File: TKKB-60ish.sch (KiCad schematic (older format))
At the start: 1 part

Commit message: EOD 12-20-20
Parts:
- removed U?: ATmega32U4-AU, Package_QFP:TQFP-44_10x10mm_P0.8mm, symbol MCU_Microchip_ATmega:ATmega32U4-AU
- added C? (x2): 27pF, Capacitor_THT:CP_Radial_D6.3mm_P2.50mm, symbol Device:C_Small
- added U?: ATmega32A-PU, Package_DIP:DIP-40_W15.24mm, symbol MCU_Microchip_ATmega:ATmega32A-PU
- added Y?: 16MHz, Crystal:Crystal_HC49-U_Vertical, symbol Device:Crystal_Small
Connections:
- net labels added: GND
- wire segments 0 -> 8
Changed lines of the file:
@@
 $EndDescr
 $Comp
-L MCU_Microchip_ATmega:ATmega32U4-AU U?
-U 1 1 5FE000C5
-P 8650 3450
-F 0 "U?" H 8650 1561 50  0000 C CNN
-F 1 "ATmega32U4-AU" H 8650 1470 50  0000 C CNN
-F 2 "Package_QFP:TQFP-44_10x10mm_P0.8mm" H 8650 3450 50  0001 C CIN
-F 3 "http://ww1.microchip.com/downloads/en/DeviceDoc/Atmel-7766-8-bit-AVR-ATmega16U4-32U4_Datasheet.pdf" H 8650 3450 50  0001 C CNN
-	1    8650 3450
+L MCU_Microchip_ATmega:ATmega32A-PU U?
+U 1 1 5FE02254
+P 9450 3400
+F 0 "U?" H 9450 1311 50  0000 C CNN
+F 1 "ATmega32A-PU" H 9450 1220 50  0000 C CNN
+F 2 "Package_DIP:DIP-40_W15.24mm" H 9450 3400 50  0001 C CIN
+F 3 "http://ww1.microchip.com/downloads/en/DeviceDoc/atmel-8155-8-bit-microcontroller-avr-atmega32a_datasheet.pdf" H 9450 3400 50  0001 C CNN
+	1    9450 3400
 	1    0    0    -1
 $EndComp
+$Comp
+L Device:Crystal_Small Y?
+U 1 1 5FE087F5
+P 8200 2000
+F 0 "Y?" V 8154 2088 50  0000 L CNN
+F 1 "16MHz" V 8245 2088 50  0000 L CNN
+F 2 "Crystal:Crystal_HC49-U_Vertical" H 8200 2000 50  0001 C CNN
+F 3 "~" H 8200 2000 50  0001 C CNN
+	1    8200 2000
+	0    1    1    0
+$EndComp
+Wire Wire Line
+	8850 1900 8200 1900
+Wire Wire Line
+	8850 2100 8200 2100
+Connection ~ 8200 1900
+Connection ~ 8200 2100
+$Comp
+L Device:C_Small C?
+U 1 1 5FE0A369
+P 7850 1800
+F 0 "C?" H 7758 1754 50  0000 R CNN
+F 1 "27pF" H 7758 1845 50  0000 R CNN
+F 2 "Capacitor_THT:CP_Radial_D6.3mm_P2.50mm" H 7850 1800 50  0001 C CNN
+F 3 "~" H 7850 1800 50  0001 C CNN
+	1    7850 1800
+	-1   0    0    1
+$EndComp
+Wire Wire Line
+	7850 1900 8200 1900
+Wire Wire Line
+	7850 2100 8200 2100
+Wire Wire Line
+	7850 1700 7700 1700
+Wire Wire Line
+	7700 1700 7700 2300
+Wire Wire Line
+	7850 2300 7700 2300
+Connection ~ 7700 2300
+Wire Wire Line
+	7700 2300 7700 2450
+$Comp
+L power:GND #PWR?
+U 1 1 5FE0CB4E
+P 7700 2450
+F 0 "#PWR?" H 7700 2200 50  0001 C CNN
+F 1 "GND" H 7705 2277 50  0000 C CNN
+F 2 "" H 7700 2450 50  0001 C CNN
+F 3 "" H 7700 2450 50  0001 C CNN
+	1    7700 2450
+	1    0    0    -1
+$EndComp
+$Comp
+L Device:C_Small C?
+U 1 1 5FE0CF1A
+P 7850 2200
+F 0 "C?" H 7758 2154 50  0000 R CNN
+F 1 "27pF" H 7758 2245 50  0000 R CNN
+F 2 "Capacitor_THT:CP_Radial_D6.3mm_P2.50mm" H 7850 2200 50  0001 C CNN
+F 3 "~" H 7850 2200 50  0001 C CNN
+	1    7850 2200
+	-1   0    0    1
+$EndComp
 $EndSCHEMATC

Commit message: Schematic Updated - still in work
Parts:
- removed C? (x2): 27pF, Capacitor_THT:CP_Radial_D6.3mm_P2.50mm, symbol Device:C_Small
- removed U?: ATmega32A-PU, Package_DIP:DIP-40_W15.24mm, symbol MCU_Microchip_ATmega:ATmega32A-PU
- removed Y?: 16MHz, Crystal:Crystal_HC49-U_Vertical, symbol Device:Crystal_Small
- added C? (x3): 0.1uF, symbol Device:C_Small
- added C?: 10uF, symbol Device:C_Small
- added D?: D_Small, symbol Device:D_Small
- added MX?: MX-NoLED, Button_Switch_Keyboard:SW_Cherry_MX_1.00u_PCB, symbol MX_Alps_Hybrid:MX-NoLED
- added R? (x2): R_Small, symbol Device:R_Small
- added U?: ATmega32U4-AU, Package_QFP:TQFP-44_10x10mm_P0.8mm, symbol MCU_Microchip_ATmega:ATmega32U4-AU
- added Y?: 16MHz, symbol Device:Crystal_Small
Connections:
- net labels added: Col0, Row0
- net labels removed: GND
- wire segments 8 -> 5
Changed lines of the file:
@@
 EESchema Schematic File Version 4
+LIBS:TKKB-60ish-cache
 EELAYER 30 0
 EELAYER END
@@
 encoding utf-8
 Sheet 1 1
-Title ""
+Title "TKKB 60ISH"
 Date ""
-Rev ""
+Rev "v0.1"
 Comp ""
-Comment1 ""
+Comment1 "by Tim Klimpel"
 Comment2 ""
 Comment3 ""
@@
 $EndDescr
 $Comp
-L MCU_Microchip_ATmega:ATmega32A-PU U?
-U 1 1 5FE02254
-P 9450 3400
-F 0 "U?" H 9450 1311 50  0000 C CNN
-F 1 "ATmega32A-PU" H 9450 1220 50  0000 C CNN
-F 2 "Package_DIP:DIP-40_W15.24mm" H 9450 3400 50  0001 C CIN
-F 3 "http://ww1.microchip.com/downloads/en/DeviceDoc/atmel-8155-8-bit-microcontroller-avr-atmega32a_datasheet.pdf" H 9450 3400 50  0001 C CNN
-	1    9450 3400
+L MCU_Microchip_ATmega:ATmega32U4-AU U?
+U 1 1 5FE50288
+P 9600 3250
+F 0 "U?" H 9600 1361 50  0000 C CNN
+F 1 "ATmega32U4-AU" H 9600 1270 50  0000 C CNN
+F 2 "Package_QFP:TQFP-44_10x10mm_P0.8mm" H 9600 3250 50  0001 C CIN
+F 3 "http://ww1.microchip.com/downloads/en/DeviceDoc/Atmel-7766-8-bit-AVR-ATmega16U4-32U4_Datasheet.pdf" H 9600 3250 50  0001 C CNN
+	1    9600 3250
 	1    0    0    -1
 $EndComp
 $Comp
+L MX_Alps_Hybrid:MX-NoLED MX?
+U 1 1 5FE574F6
+P 1250 1600
+F 0 "MX?" H 1283 1823 60  0000 C CNN
+F 1 "MX-NoLED" H 1283 1749 20  0000 C CNN
+F 2 "Button_Switch_Keyboard:SW_Cherry_MX_1.00u_PCB" H 625 1575 60  0001 C CNN
+F 3 "" H 625 1575 60  0001 C CNN
+	1    1250 1600
+	1    0    0    -1
+$EndComp
+$Comp
+L Device:D_Small D?
+U 1 1 5FE5851E
+P 1200 2000
+F 0 "D?" V 1246 1932 50  0000 R CNN
+F 1 "D_Small" V 1155 1932 50  0000 R CNN
+F 2 "" V 1200 2000 50  0001 C CNN
+F 3 "~" V 1200 2000 50  0001 C CNN
+	1    1200 2000
+	0    -1   -1   0
+$EndComp
+Wire Wire Line
+	1200 1750 1200 1900
+Wire Wire Line
+	1400 1550 1750 1550
+Wire Wire Line
+	1200 2100 1200 2250
+Text GLabel 1750 1250 1    50   Input ~ 0
+Col0
+Wire Wire Line
+	1750 1550 1750 1250
+Text GLabel 1050 2250 0    50   Input ~ 0
+Row0
+Wire Wire Line
+	1200 2250 1050 2250
+$Comp
 L Device:Crystal_Small Y?
-U 1 1 5FE087F5
-P 8200 2000
-F 0 "Y?" V 8154 2088 50  0000 L CNN
-F 1 "16MHz" V 8245 2088 50  0000 L CNN
-F 2 "Crystal:Crystal_HC49-U_Vertical" H 8200 2000 50  0001 C CNN
-F 3 "~" H 8200 2000 50  0001 C CNN
-	1    8200 2000
+U 1 1 5FE5B267
+P 8450 2050
+F 0 "Y?" H 8450 2275 50  0000 C CNN
+F 1 "16MHz" H 8450 2184 50  0000 C CNN
+F 2 "" H 8450 2050 50  0001 C CNN
+F 3 "~" H 8450 2050 50  0001 C CNN
+	1    8450 2050
+	1    0    0    -1
+$EndComp
+$Comp
+L Device:R_Small R?
+U 1 1 5FE5BC3F
+P 8450 2750
+F 0 "R?" V 8254 2750 50  0000 C CNN
+F 1 "R_Small" V 8345 2750 50  0000 C CNN
+F 2 "" H 8450 2750 50  0001 C CNN
+F 3 "~" H 8450 2750 50  0001 C CNN
+	1    8450 2750
 	0    1    1    0
 $EndComp
-Wire Wire Line
-	8850 1900 8200 1900
-Wire Wire Line
-	8850 2100 8200 2100
-Connection ~ 8200 1900
-Connection ~ 8200 2100
+$Comp
+L Device:R_Small R?
+U 1 1 5FE5C705
+P 8150 2850
+F 0 "R?" V 7954 2850 50  0000 C CNN
+F 1 "R_Small" V 8045 2850 50  0000 C CNN
+F 2 "" H 8150 2850 50  0001 C CNN
+F 3 "~" H 8150 2850 50  0001 C CNN
+	1    8150 2850
+	0    1    1    0
+$EndComp
 $Comp
 L Device:C_Small C?
-U 1 1 5FE0A369
-P 7850 1800
-F 0 "C?" H 7758 1754 50  0000 R CNN
-F 1 "27pF" H 7758 1845 50  0000 R CNN
-F 2 "Capacitor_THT:CP_Radial_D6.3mm_P2.50mm" H 7850 1800 50  0001 C CNN
-F 3 "~" H 7850 1800 50  0001 C CNN
-	1    7850 1800
-	-1   0    0    1
-$EndComp
-Wire Wire Line
-	7850 1900 8200 1900
-Wire Wire Line
-	7850 2100 8200 2100
-Wire Wire Line
-	7850 1700 7700 1700
-Wire Wire Line
-	7700 1700 7700 2300
-Wire Wire Line
-	7850 2300 7700 2300
-Connection ~ 7700 2300
-Wire Wire Line
-	7700 2300 7700 2450
-$Comp
-L power:GND #PWR?
-U 1 1 5FE0CB4E
-P 7700 2450
-F 0 "#PWR?" H 7700 2200 50  0001 C CNN
-F 1 "GND" H 7705 2277 50  0000 C CNN
-F 2 "" H 7700 2450 50  0001 C CNN
-F 3 "" H 7700 2450 50  0001 C CNN
-	1    7700 2450
+U 1 1 5FE5E1A9
+P 8650 850
+F 0 "C?" H 8742 896 50  0000 L CNN
+F 1 "0.1uF" H 8742 805 50  0000 L CNN
+F 2 "" H 8650 850 50  0001 C CNN
+F 3 "~" H 8650 850 50  0001 C CNN
+	1    8650 850
 	1    0    0    -1
 $EndComp
 $Comp
 L Device:C_Small C?
-U 1 1 5FE0CF1A
-P 7850 2200
-F 0 "C?" H 7758 2154 50  0000 R CNN
-F 1 "27pF" H 7758 2245 50  0000 R CNN
-F 2 "Capacitor_THT:CP_Radial_D6.3mm_P2.50mm" H 7850 2200 50  0001 C CNN
-F 3 "~" H 7850 2200 50  0001 C CNN
-	1    7850 2200
-	-1   0    0    1
+U 1 1 5FE5F023
+P 9150 850
+F 0 "C?" H 9242 896 50  0000 L CNN
+F 1 "0.1uF" H 9242 805 50  0000 L CNN
+F 2 "" H 9150 850 50  0001 C CNN
+F 3 "~" H 9150 850 50  0001 C CNN
+	1    9150 850
+	1    0    0    -1
+$EndComp
+$Comp
+L Device:C_Small C?
+U 1 1 5FE5F306
+P 9650 850
+F 0 "C?" H 9742 896 50  0000 L CNN
+F 1 "0.1uF" H 9742 805 50  0000 L CNN
+F 2 "" H 9650 850 50  0001 C CNN
+F 3 "~" H 9650 850 50  0001 C CNN
+	1    9650 850
+	1    0    0    -1
+$EndComp
+$Comp
+L Device:C_Small C?
+U 1 1 5FE5F4FA
+P 10150 850
+F 0 "C?" H 10242 896 50  0000 L CNN
+F 1 "10uF" H 10242 805 50  0000 L CNN
+F 2 "" H 10150 850 50  0001 C CNN
+F 3 "~" H 10150 850 50  0001 C CNN
+	1    10150 850
+	1    0    0    -1
 $EndComp
 $EndSCHEMATC

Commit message: Add Type-c pretty
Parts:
- added USB?: Wurth-632723300011, symbol Type-C:Wurth-632723300011
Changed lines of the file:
@@
+	1    0    0    -1
+$EndComp
+$Comp
+L Type-C:Wurth-632723300011 USB?
+U 1 1 5FF07F7B
+P 5950 2950
+F 0 "USB?" H 5562 4347 60  0000 C CNN
+F 1 "Wurth-632723300011" H 5562 4241 60  0000 C CNN
+F 2 "" H 5950 2950 60  0001 C CNN
+F 3 "" H 5950 2950 60  0001 C CNN
+	1    5950 2950
 	1    0    0    -1
 $EndComp

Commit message: Added USB/Boot/ISP/Init MCU to schematic
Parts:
- removed C? (x3): 0.1uF, symbol Device:C_Small
- removed C?: 10uF, symbol Device:C_Small
- removed D?: D_Small, symbol Device:D_Small
- removed MX?: MX-NoLED, Button_Switch_Keyboard:SW_Cherry_MX_1.00u_PCB, symbol MX_Alps_Hybrid:MX-NoLED
- removed R? (x2): R_Small, symbol Device:R_Small
- removed U?: ATmega32U4-AU, Package_QFP:TQFP-44_10x10mm_P0.8mm, symbol MCU_Microchip_ATmega:ATmega32U4-AU
- removed USB?: Wurth-632723300011, symbol Type-C:Wurth-632723300011
- added Boot?: Boot, Button_Switch_THT:SW_PUSH_6mm, symbol Switch:SW_Push
- added C? (x2): 22p, symbol Device:C_Small
- added D? (x2): 3.6V, symbol Device:D_Zener_Small
- added F?: 500mA, symbol Device:Polyfuse_Small
- added J?: AVR-ISP-6, Connector_PinHeader_1.00mm:PinHeader_2x03_P1.00mm_Vertical, symbol Connector:AVR-ISP-6
- added R? (x2): 75R, symbol Device:R_Small
- added R? (x2): 5k1, symbol Device:R_Small
- added R?: 10k, symbol Device:R_Small
- added Reset?: Reset, Button_Switch_THT:SW_PUSH_6mm, symbol Switch:SW_Push
- added U?: ATmega32A-PU, Package_DIP:DIP-40_W15.24mm, symbol MCU_Microchip_ATmega:ATmega32A-PU
- added USB?: Type-C_USB_C_GCT_USB4085, Connector_USB:USB_C_Receptacle_GCT_USB4085, symbol Type-C:Type-C_USB_C_GCT_USB4085
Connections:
- net labels added: +5V, Boot, D+, D-, GND, MISO, MOSI, Reset, SCK, USB_CC, USB_Vbus
- net labels removed: Col0, Row0
- wire segments 5 -> 62
- no-connect marks 0 -> 3
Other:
- note added: "Boot/Rst\n"
- note added: "ISP\n"
- note added: "USB\n"
- moved on the sheet: Y?

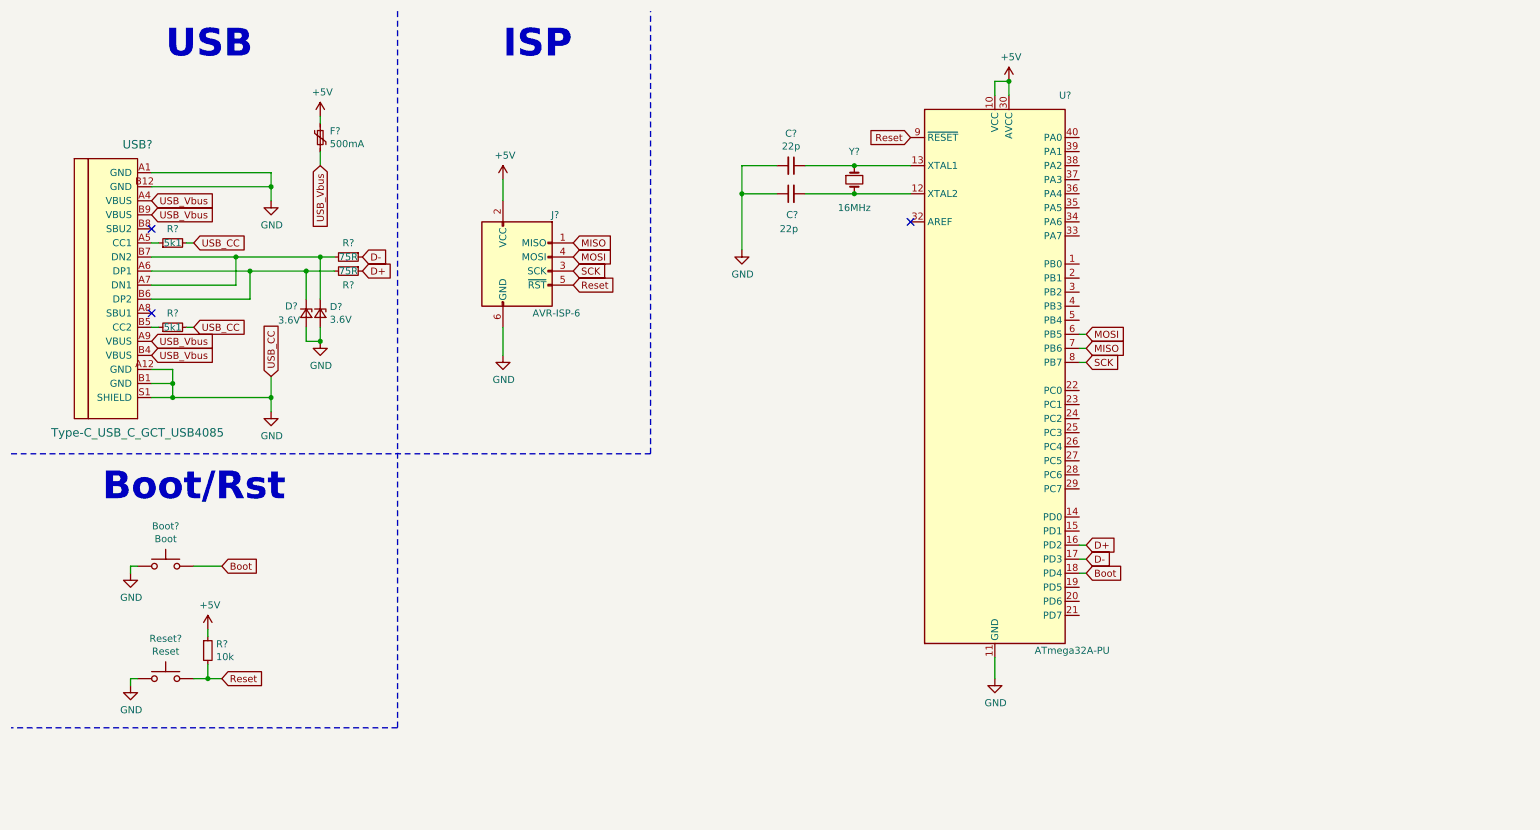
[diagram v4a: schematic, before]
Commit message: PCB Layout edits
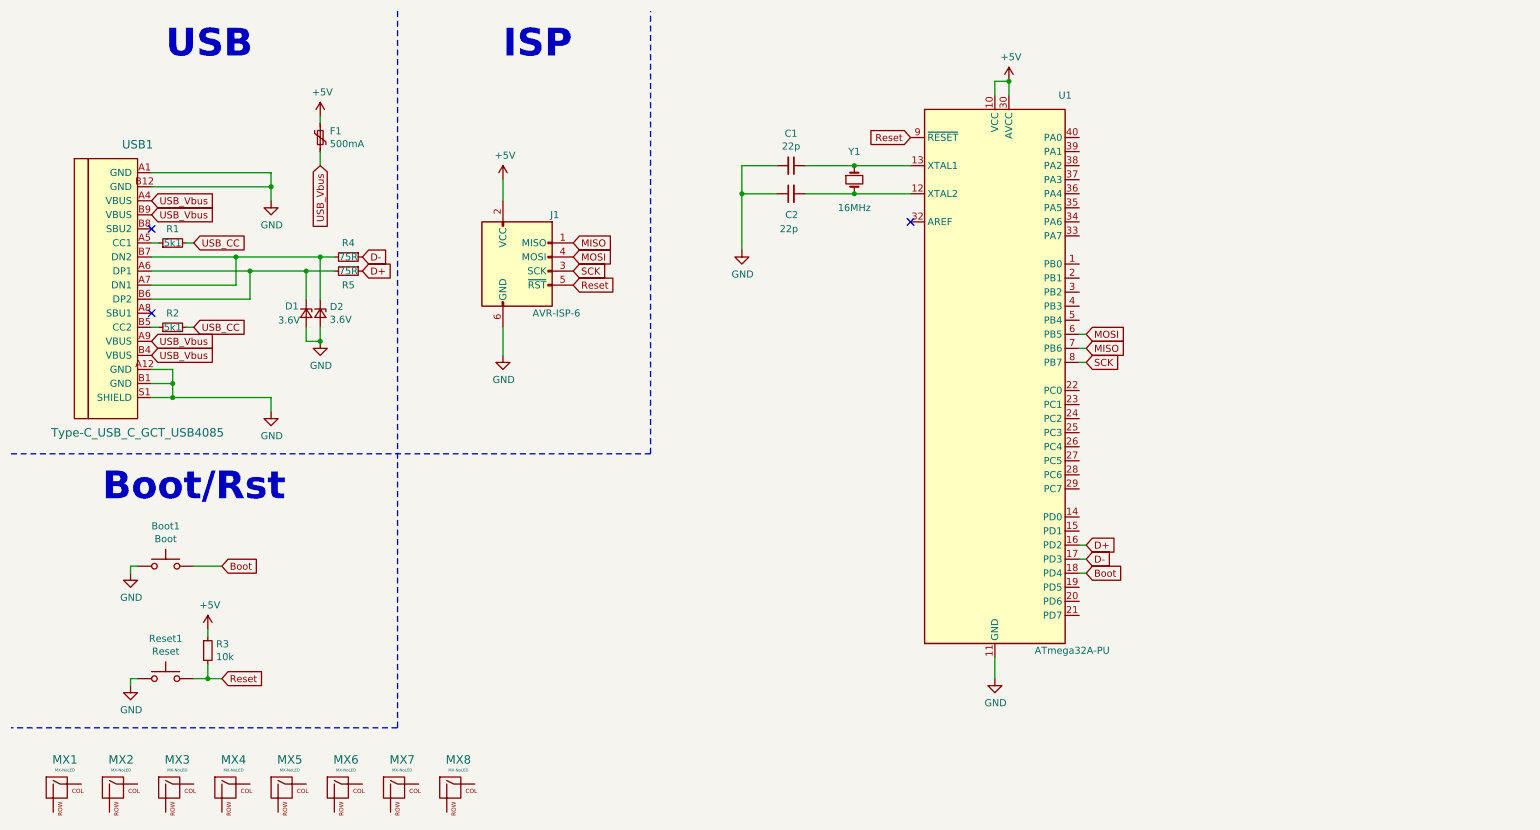
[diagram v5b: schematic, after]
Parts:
- added MX1, MX2, MX3, MX4, MX5, MX6, MX7, MX8: MX-NoLED, Button_Switch_Keyboard:SW_Cherry_MX_1.00u_PCB, symbol MX_Alps_Hybrid:MX-NoLED
- C1, C2: renamed from C?; footprint (none) -> Capacitor_THT:CP_Radial_D5.0mm_P2.00mm
- D1, D2: renamed from D?; footprint (none) -> Diode_THT:D_DO-35_SOD27_P7.62mm_Horizontal
- F1: renamed from F?; footprint (none) -> Fuse:Fuse_BelFuse_0ZRE0005FF_L8.3mm_W3.8mm
- R1, R2, R3, R4, R5: renamed from R?; footprint (none) -> Resistor_THT:R_Axial_DIN0204_L3.6mm_D1.6mm_P7.62mm_Horizontal
- Y1: renamed from Y?; footprint (none) -> Crystal:Crystal_HC49-U_Vertical
- gave numbers to parts that had none: 5
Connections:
- net GND: no longer R1.2, R2.2
- new net USB_CC: R1.2, R2.2

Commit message: Updated Schematic
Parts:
- removed MX1, MX2, MX3, MX4, MX5, MX6, MX7, MX8: MX-NoLED, Button_Switch_Keyboard:SW_Cherry_MX_1.00u_PCB, symbol MX_Alps_Hybrid:MX-NoLED
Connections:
- net USB_CC is gone; now on net GND: R1.2, R2.2
- net Row_0: now reaches U1.1 (PB0)
- net Row_1: now reaches U1.2 (PB1)
- net Row_2: now reaches U1.3 (PB2)
- net Col_7: now reaches U1.33 (PA7)
- net Col_6: now reaches U1.34 (PA6)
- net Col_5: now reaches U1.35 (PA5)
- net Col_4: now reaches U1.36 (PA4)
- net Col_3: now reaches U1.37 (PA3)
- net Col_2: now reaches U1.38 (PA2)
- net Col_1: now reaches U1.39 (PA1)
- net Col_0: now reaches U1.40 (PA0)
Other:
- moved on the sheet: C1, C2, U1, Y1

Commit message: update to kicad schematic and pcb
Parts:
- added C3: 4u7, Capacitor_THT:CP_Radial_D5.0mm_P2.00mm, symbol Device:CP1_Small
- added C4, C5: 0u1, Capacitor_THT:C_Disc_D5.1mm_W3.2mm_P5.00mm, symbol Device:C_Small
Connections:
- net +5V: now also C3.1, C4.1, C5.1
- net GND: now also C3.2, C4.2, C5.2
- net Row_5: now reaches U1.22 (PC0)
- net Row_6: now reaches U1.23 (PC1)
- net Row_7: now reaches U1.24 (PC2)
- net Row_8: now reaches U1.25 (PC3)
- net Row_9: now reaches U1.26 (PC4)
- net Row_10: now reaches U1.27 (PC5)
- net Row_11: now reaches U1.28 (PC6)
- net Row_3: now reaches U1.4 (PB3)
- net Row_4: now reaches U1.5 (PB4)
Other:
- note added: "MCU\n"
- note added: "Power\n"
- note added: "Sw Matrix\n"
- moved on the sheet: C1, C2, F1, U1, Y1

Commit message: Board layout work
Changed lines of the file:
@@
 Text GLabel 10300 1600 2    50   Input ~ 0
 Col_0
-Text GLabel 6700 1700 2    50   Input ~ 0
+Text GLabel 6700 1700 2    50   BiDi ~ 0
 Col_0
 Text GLabel 10300 1700 2    50   Input ~ 0
@@
 Text GLabel 10300 2300 2    50   Input ~ 0
 Col_7
-Text GLabel 6700 1800 2    50   Input ~ 0
+Text GLabel 6700 1800 2    50   BiDi ~ 0
 Col_1
-Text GLabel 6700 1900 2    50   Input ~ 0
+Text GLabel 6700 1900 2    50   BiDi ~ 0
 Col_2
-Text GLabel 6700 2000 2    50   Input ~ 0
+Text GLabel 6700 2000 2    50   BiDi ~ 0
 Col_3
-Text GLabel 6700 2100 2    50   Input ~ 0
+Text GLabel 6700 2100 2    50   BiDi ~ 0
 Col_4
-Text GLabel 6700 2200 2    50   Input ~ 0
+Text GLabel 6700 2200 2    50   BiDi ~ 0
 Col_5
-Text GLabel 6700 2300 2    50   Input ~ 0
+Text GLabel 6700 2300 2    50   BiDi ~ 0
 Col_6
-Text GLabel 6700 2400 2    50   Input ~ 0
+Text GLabel 6700 2400 2    50   BiDi ~ 0
 Col_7
 Wire Wire Line
